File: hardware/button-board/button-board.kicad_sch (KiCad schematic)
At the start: 9 parts, among them J2 BUTTON, J3 BUTTON, J7 Big button

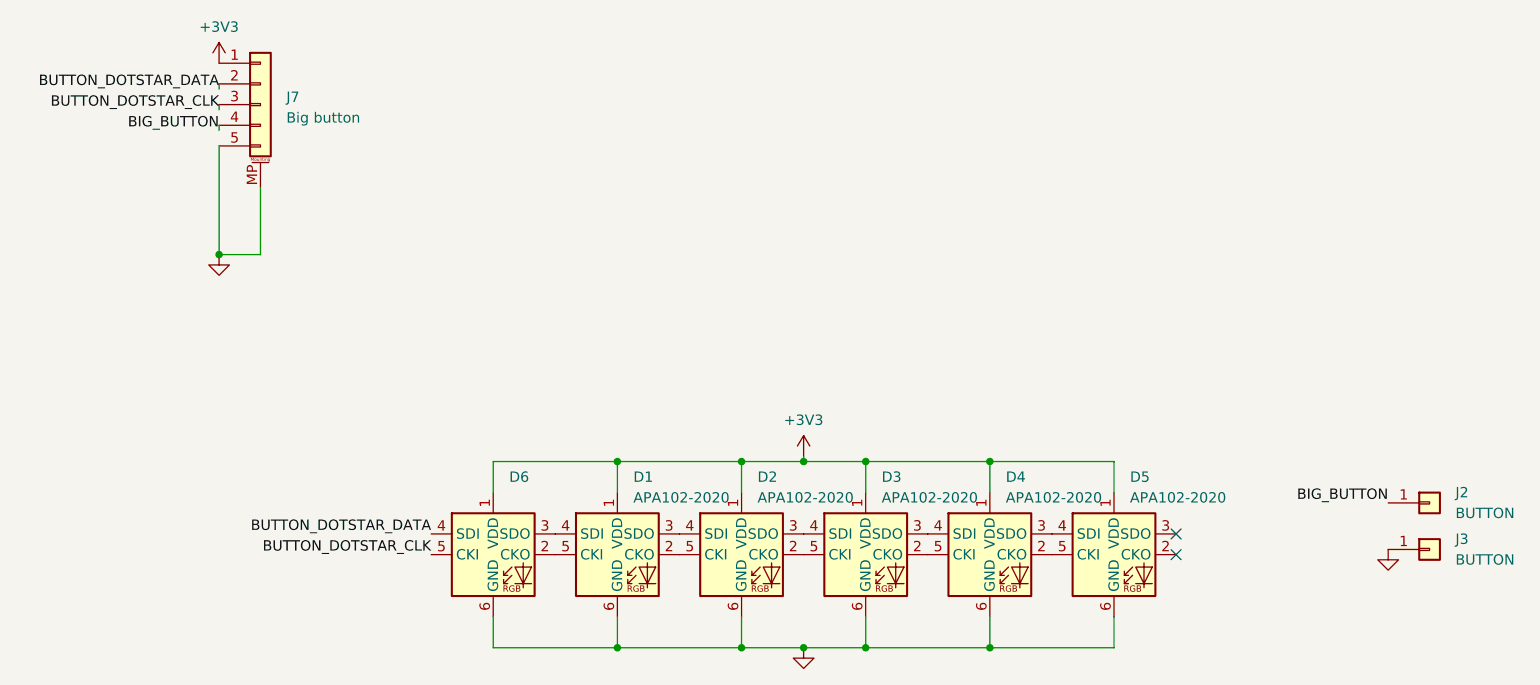
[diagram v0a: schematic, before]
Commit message: hardware: Revise button board- move all components to front side, update footprint for LEDs, add caps, change friction tabs to avoid interference with switch locking tabs
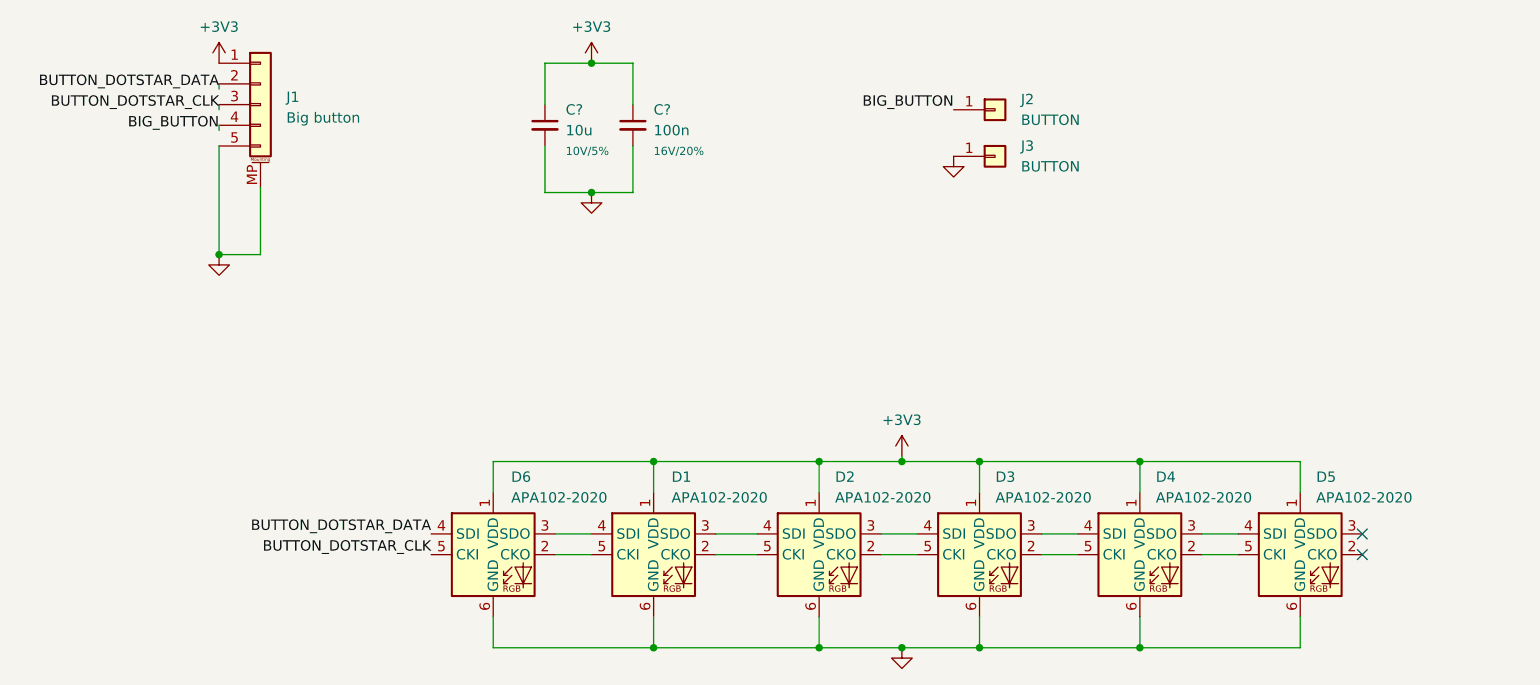
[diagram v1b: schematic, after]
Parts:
- added C?: 10u, winterbloom:C_0603_HandSolder, symbol Device:C_Small
- added C?: 100n, winterbloom:C_0603_HandSolder, symbol Device:C_Small
- D1, D2, D3, D4, D5, D6: footprint LED_SMD:LED-APA102-2020 -> winterbloom:LED-APA102-2020
- renumbered J7 to J1
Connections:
- net +3V3: now also C?.1, C?.1
- net GND: now also C?.2, C?.2
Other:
- moved on the sheet: D1, D2, D3, D4, D5, J2, J3
